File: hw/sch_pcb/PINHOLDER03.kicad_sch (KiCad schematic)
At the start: 8 parts, among them J1 HEADER_1x03, M1 HOLE, M2 HOLE, M3 HOLE, M4 HOLE

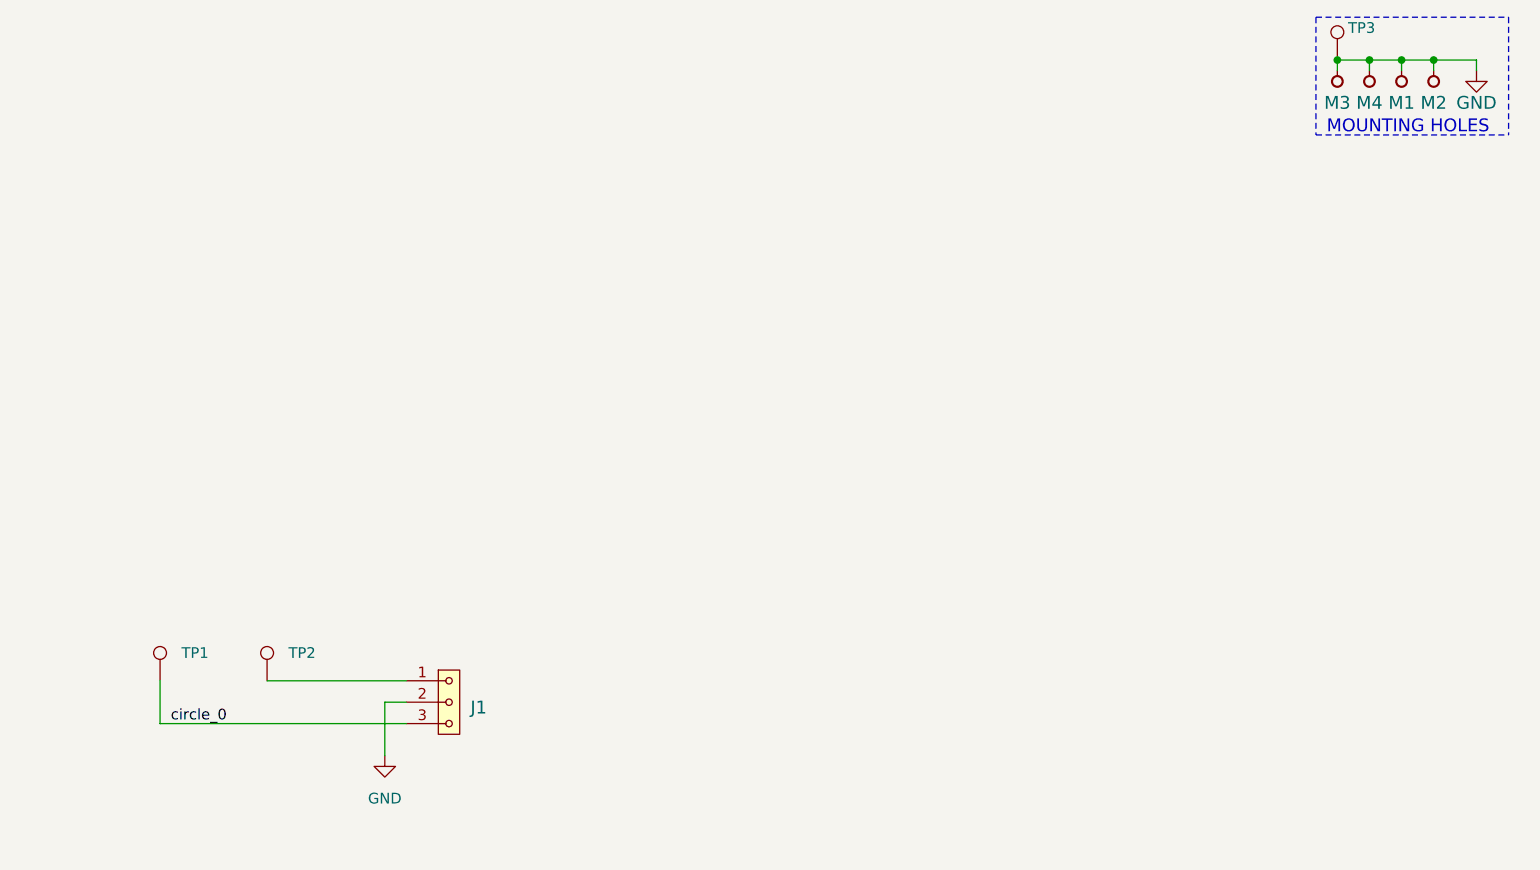
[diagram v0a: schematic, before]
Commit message: uprava layoutu, 2 diody
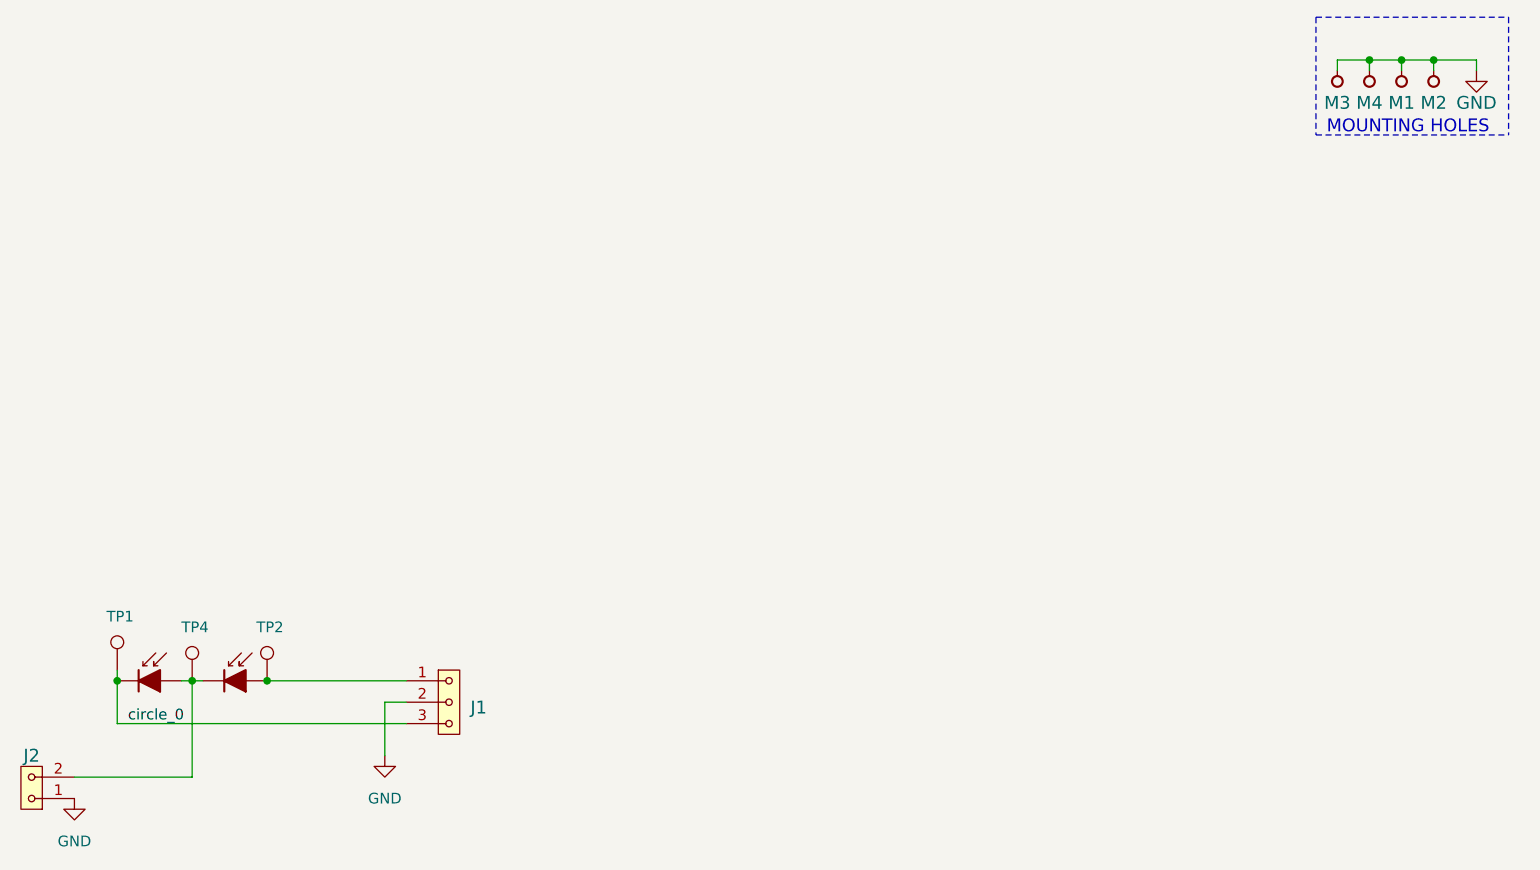
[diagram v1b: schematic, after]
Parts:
- removed TP3: TestPoint, Mlab_CON:TestPoint_Pad_D0.5mm_noSilk, symbol Connector:TestPoint
- added D1, D2: D_Photo_Filled, symbol Device:D_Photo_Filled
- added J2: HEADER_1x02, Mlab_Pin_Headers:Straight_1x02, symbol MLAB_HEADER:HEADER_1x02
- added TP4: TestPoint, Mlab_CON:TestPoint_Pad_D0.5mm_noSilk, symbol Connector:TestPoint
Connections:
- net GND: now also J2.1
- net circle_0: now also D1.1 (K)
- net at J1.1, TP2.1: now also D2.2 (A)
- new net: D1.2 (A), D2.1 (K), J2.2, TP4.1
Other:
- moved on the sheet: TP1
